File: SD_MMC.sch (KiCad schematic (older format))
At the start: 14 parts, among them J3 Micro_SD_Card, U1 MIMX8MM6DVTLZAA, U5 SDINBDG4-8G

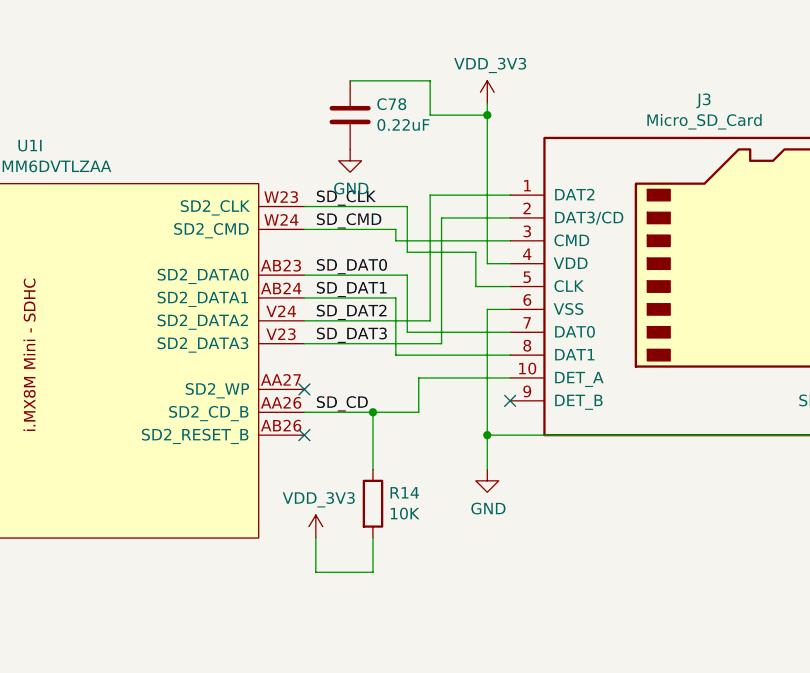
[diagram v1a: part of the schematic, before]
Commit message: Add esd protection for usb
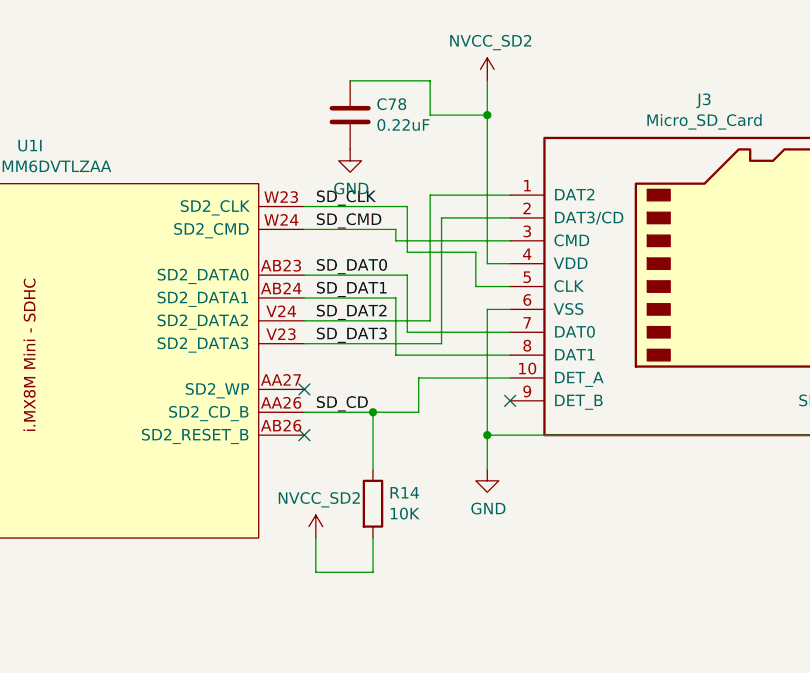
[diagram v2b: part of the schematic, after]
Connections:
- net VDD_3V3: no longer C78.1, J3.4 (VDD), R14.2
- new net NVCC_SD2: C78.1, J3.4 (VDD), R14.2
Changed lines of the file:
@@
 	1    0    0    -1
 $EndComp
-$Comp
-L mxenc:VDD_3V3 #PWR0142
-U 1 1 5D204D73
-P 10200 4150
-F 0 "#PWR0142" H 10200 4000 50  0001 C CNN
-F 1 "VDD_3V3" H 10215 4323 50  0000 C CNN
-F 2 "" H 10200 4150 50  0001 C CNN
-F 3 "" H 10200 4150 50  0001 C CNN
-	1    10200 4150
-	1    0    0    -1
-$EndComp
-Wire Wire Line
-	10200 4150 10200 4200
 Wire Wire Line
 	10200 4850 10300 4850
@@
 Wire Wire Line
 	9700 5750 9700 5500
-$Comp
-L mxenc:VDD_3V3 #PWR0144
-U 1 1 5D211DBD
-P 9450 6050
-F 0 "#PWR0144" H 9450 5900 50  0001 C CNN
-F 1 "VDD_3V3" H 9465 6223 50  0000 C CNN
-F 2 "" H 9450 6050 50  0001 C CNN
-F 3 "" H 9450 6050 50  0001 C CNN
-	1    9450 6050
-	1    0    0    -1
-$EndComp
 Wire Wire Line
 	9450 6050 9450 6200
@@
 NoConn ~ 9400 5400
 NoConn ~ 10300 5450
+$Comp
+L mxenc:NVCC_SD2 #PWR0144
+U 1 1 5DC50CF4
+P 10200 4050
+F 0 "#PWR0144" H 10200 3900 50  0001 C CNN
+F 1 "NVCC_SD2" H 10215 4223 50  0000 C CNN
+F 2 "" H 10200 4050 50  0001 C CNN
+F 3 "" H 10200 4050 50  0001 C CNN
+	1    10200 4050
+	1    0    0    -1
+$EndComp
+Wire Wire Line
+	10200 4050 10200 4200
+$Comp
+L mxenc:NVCC_SD2 #PWR0243
+U 1 1 5DC5A2D8
+P 9450 6050
+F 0 "#PWR0243" H 9450 5900 50  0001 C CNN
+F 1 "NVCC_SD2" H 9465 6223 50  0000 C CNN
+F 2 "" H 9450 6050 50  0001 C CNN
+F 3 "" H 9450 6050 50  0001 C CNN
+	1    9450 6050
+	1    0    0    -1
+$EndComp
 $EndSCHEMATC

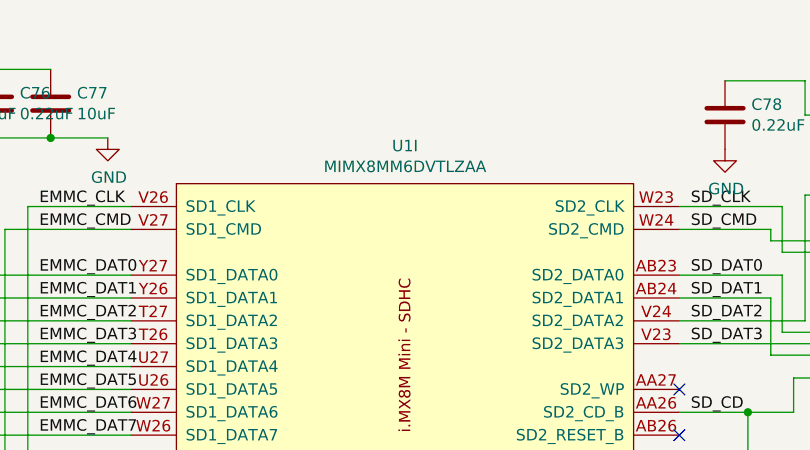
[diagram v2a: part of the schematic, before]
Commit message: Complete entry of bom
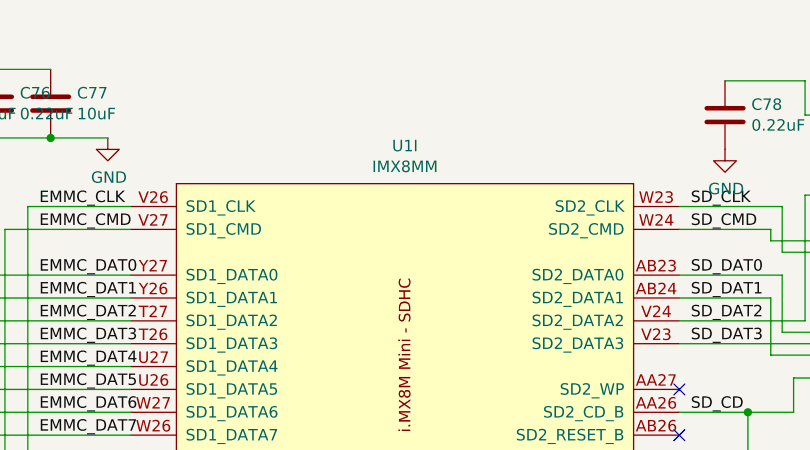
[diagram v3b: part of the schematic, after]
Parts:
- C71: Mfgr (none) -> Murata; Part (none) -> GRM155C80J475MEAAD; Vendorpart (none) -> 490-14458-1-ND
- C72, C73, C74, C75, C76, C80: Mfgr (none) -> Murata; Part (none) -> GRM033C80J224KE90D; Vendorpart (none) -> 490-10392-1-ND
- C77: Mfgr (none) -> Murata; Part (none) -> GRM155C80J106ME11D; Vendorpart (none) -> 490-13233-1-ND
- C78: Mfgr (none) -> Murata; Part (none) -> GRM155C8YA224ME01D; Vendorpart (none) -> 490-10446-1-ND
- C79: Mfgr (none) -> Murata; Part (none) -> GRM155C81A105KA12D; Vendorpart (none) -> 490-12699-1-ND
- J3: Mfgr (none) -> Amphenol; Part (none) -> 114-00841-68; Vendorpart (none) -> 114-00841-68-1-ND
- R14: Mfgr (none) -> Panasonic; Part (none) -> ERJ-2GEJ103X; Vendorpart (none) -> P10KJCT-ND
- U1: value MIMX8MM6DVTLZAA -> IMX8MM; Mfgr (none) -> NXP; Part (none) -> MIMX8MM6CVTKZAA; Vendorpart (none) -> 568-15276-ND
- U5: Field4 SDINBDG4-8G -> (none); Field5 SanDisk -> (none); Field6 Unavailable -> (none); Field7 USB Flash Drives 8GB 3.3V -> (none); Field8 None -> (none); Mfgr (none) -> SanDisk; Part (none) -> SDINBDG4-8G-I1; Vendor (none) -> Mouser; Vendorpart (none) -> 467-SDINBDG4-8G-I1
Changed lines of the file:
@@
 P 8200 7200
 F 0 "U1" H 8200 10065 50  0000 C CNN
-F 1 "MIMX8MM6DVTLZAA" H 8200 9974 50  0000 C CNN
+F 1 "IMX8MM" H 8200 9974 50  0000 C CNN
 F 2 "mxenc:BGA-729_27x27_14.0x14.0mm" H 8450 9950 50  0001 C CNN
 F 3 "" H 7450 9950 50  0001 C CNN
+F 4 "NXP" H 8200 7200 50  0001 C CNN "Mfgr"
+F 5 "MIMX8MM6CVTKZAA" H 8200 7200 50  0001 C CNN "Part"
+F 6 "568-15276-ND" H 8200 7200 50  0001 C CNN "Vendorpart"
 	9    8200 7200
 	1    0    0    -1
@@
 F 2 "mxenc:BGA153C50P14X14_1300X1150X80N" H 4950 5500 50  0001 L BNN
 F 3 "" H 4950 5500 50  0001 L BNN
-F 4 "SDINBDG4-8G" H 4950 5500 50  0001 L BNN "Field4"
-F 5 "SanDisk" H 4950 5500 50  0001 L BNN "Field5"
-F 6 "Unavailable" H 4950 5500 50  0001 L BNN "Field6"
-F 7 "USB Flash Drives 8GB 3.3V" H 4950 5500 50  0001 L BNN "Field7"
-F 8 "None" H 4950 5500 50  0001 L BNN "Field8"
+F 4 "SanDisk" H 4950 5500 50  0001 C CNN "Mfgr"
+F 5 "SDINBDG4-8G-I1" H 4950 5500 50  0001 C CNN "Part"
+F 6 "Mouser" H 4950 5500 50  0001 C CNN "Vendor"
+F 7 "467-SDINBDG4-8G-I1" H 4950 5500 50  0001 C CNN "Vendorpart"
 	1    4950 5500
 	1    0    0    -1
@@
 F 2 "Resistor_SMD:R_0402_1005Metric" V 9630 5900 50  0001 C CNN
 F 3 "~" H 9700 5900 50  0001 C CNN
+F 4 "Panasonic" H 9700 5900 50  0001 C CNN "Mfgr"
+F 5 "ERJ-2GEJ103X" H 9700 5900 50  0001 C CNN "Part"
+F 6 "P10KJCT-ND" H 9700 5900 50  0001 C CNN "Vendorpart"
 	1    9700 5900
 	1    0    0    -1
@@
 F 2 "Capacitor_SMD:C_0402_1005Metric" H 9638 4050 50  0001 C CNN
 F 3 "~" H 9600 4200 50  0001 C CNN
+F 4 "Murata" H 9600 4200 50  0001 C CNN "Mfgr"
+F 5 "GRM155C8YA224ME01D" H 9600 4200 50  0001 C CNN "Part"
+F 6 "490-10446-1-ND" H 9600 4200 50  0001 C CNN "Vendorpart"
 	1    9600 4200
 	1    0    0    -1
@@
 F 2 "Capacitor_SMD:C_0201_0603Metric" H 5888 4000 50  0001 C CNN
 F 3 "~" H 5850 4150 50  0001 C CNN
+F 4 "Murata" H 5850 4150 50  0001 C CNN "Mfgr"
+F 5 "GRM033C80J224KE90D" H 5850 4150 50  0001 C CNN "Part"
+F 6 "490-10392-1-ND" H 5850 4150 50  0001 C CNN "Vendorpart"
 	1    5850 4150
 	1    0    0    -1
@@
 F 2 "Capacitor_SMD:C_0201_0603Metric" H 6188 4000 50  0001 C CNN
 F 3 "~" H 6150 4150 50  0001 C CNN
+F 4 "Murata" H 6150 4150 50  0001 C CNN "Mfgr"
+F 5 "GRM033C80J224KE90D" H 6150 4150 50  0001 C CNN "Part"
+F 6 "490-10392-1-ND" H 6150 4150 50  0001 C CNN "Vendorpart"
 	1    6150 4150
 	1    0    0    -1
@@
 F 2 "Capacitor_SMD:C_0201_0603Metric" H 6438 4000 50  0001 C CNN
 F 3 "~" H 6400 4150 50  0001 C CNN
+F 4 "Murata" H 6400 4150 50  0001 C CNN "Mfgr"
+F 5 "GRM033C80J224KE90D" H 6400 4150 50  0001 C CNN "Part"
+F 6 "490-10392-1-ND" H 6400 4150 50  0001 C CNN "Vendorpart"
 	1    6400 4150
 	1    0    0    -1
@@
 F 2 "Capacitor_SMD:C_0402_1005Metric" H 6688 4000 50  0001 C CNN
 F 3 "~" H 6650 4150 50  0001 C CNN
+F 4 "Murata" H 6650 4150 50  0001 C CNN "Mfgr"
+F 5 "GRM155C80J106ME11D" H 6650 4150 50  0001 C CNN "Part"
+F 6 "490-13233-1-ND" H 6650 4150 50  0001 C CNN "Vendorpart"
 	1    6650 4150
 	1    0    0    -1
@@
 F 2 "Capacitor_SMD:C_0201_0603Metric" H 4138 4000 50  0001 C CNN
 F 3 "~" H 4100 4150 50  0001 C CNN
+F 4 "Murata" H 4100 4150 50  0001 C CNN "Mfgr"
+F 5 "GRM033C80J224KE90D" H 4100 4150 50  0001 C CNN "Part"
+F 6 "490-10392-1-ND" H 4100 4150 50  0001 C CNN "Vendorpart"
 	1    4100 4150
 	1    0    0    -1
@@
 F 2 "Capacitor_SMD:C_0201_0603Metric" H 3888 4000 50  0001 C CNN
 F 3 "~" H 3850 4150 50  0001 C CNN
+F 4 "Murata" H 3850 4150 50  0001 C CNN "Mfgr"
+F 5 "GRM033C80J224KE90D" H 3850 4150 50  0001 C CNN "Part"
+F 6 "490-10392-1-ND" H 3850 4150 50  0001 C CNN "Vendorpart"
 	1    3850 4150
 	1    0    0    -1
@@
 F 2 "Capacitor_SMD:C_0402_1005Metric" H 3638 4000 50  0001 C CNN
 F 3 "~" H 3600 4150 50  0001 C CNN
+F 4 "Murata" H 3600 4150 50  0001 C CNN "Mfgr"
+F 5 "GRM155C80J475MEAAD" H 3600 4150 50  0001 C CNN "Part"
+F 6 "490-14458-1-ND" H 3600 4150 50  0001 C CNN "Vendorpart"
 	1    3600 4150
 	1    0    0    -1
@@
 F 2 "Capacitor_SMD:C_0201_0603Metric" H 3688 5000 50  0001 C CNN
 F 3 "~" H 3650 5150 50  0001 C CNN
+F 4 "Murata" H 3650 5150 50  0001 C CNN "Mfgr"
+F 5 "GRM033C80J224KE90D" H 3650 5150 50  0001 C CNN "Part"
+F 6 "490-10392-1-ND" H 3650 5150 50  0001 C CNN "Vendorpart"
 	1    3650 5150
 	1    0    0    -1
@@
 F 2 "Capacitor_SMD:C_0402_1005Metric" H 3438 5000 50  0001 C CNN
 F 3 "~" H 3400 5150 50  0001 C CNN
+F 4 "Murata" H 3400 5150 50  0001 C CNN "Mfgr"
+F 5 "GRM155C81A105KA12D" H 3400 5150 50  0001 C CNN "Part"
+F 6 "490-12699-1-ND" H 3400 5150 50  0001 C CNN "Vendorpart"
 	1    3400 5150
 	1    0    0    -1
@@
 F 2 "mxenc:114-00841-68" H 12350 5250 50  0001 C CNN
 F 3 "http://katalog.we-online.de/em/datasheet/693072010801.pdf" H 11200 4950 50  0001 C CNN
+F 4 "Amphenol" H 11200 4950 50  0001 C CNN "Mfgr"
+F 5 "114-00841-68" H 11200 4950 50  0001 C CNN "Part"
+F 6 "114-00841-68-1-ND" H 11200 4950 50  0001 C CNN "Vendorpart"
 	1    11200 4950
 	1    0    0    -1

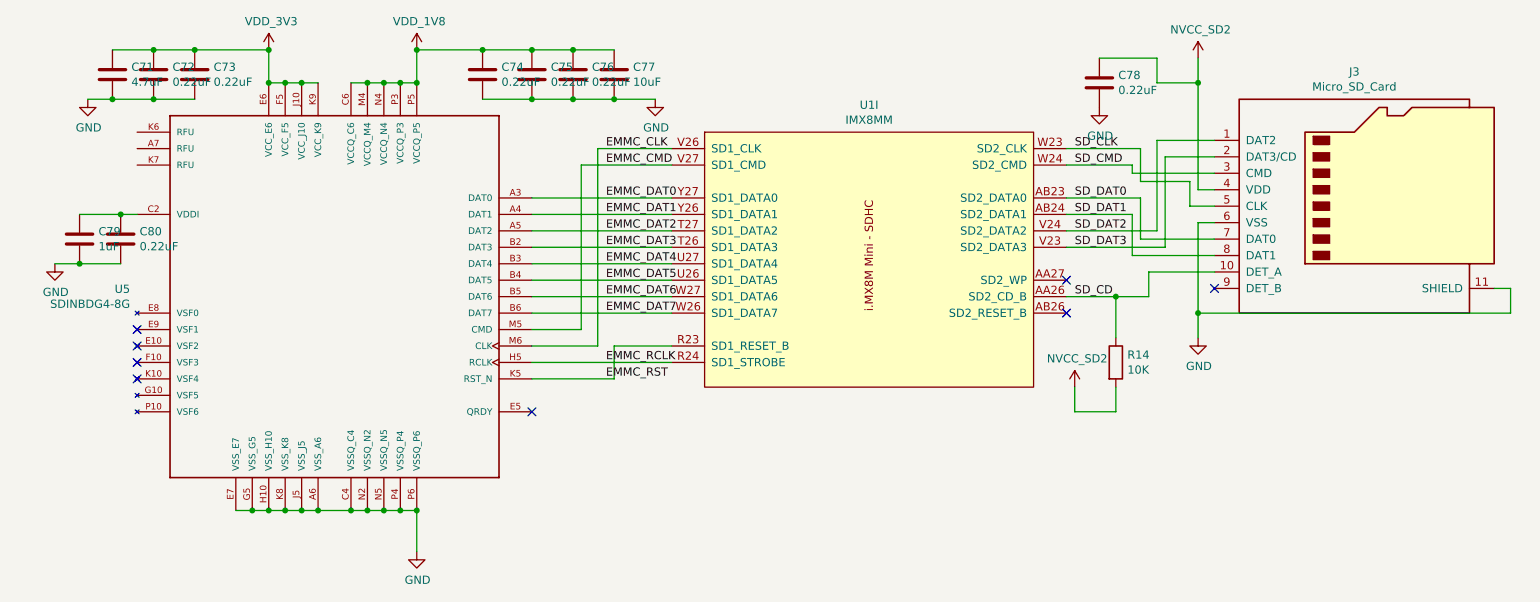
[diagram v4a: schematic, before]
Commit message: rough layout, routing for emmc and csi, dsi, pcie
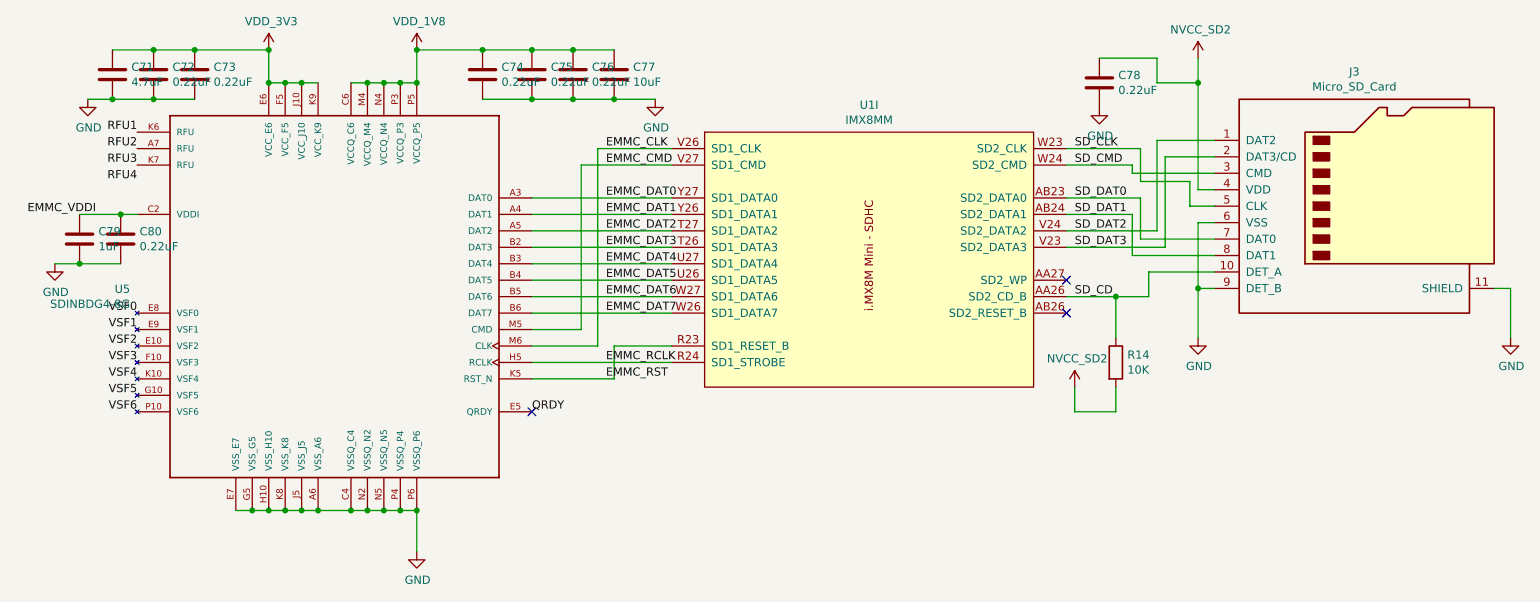
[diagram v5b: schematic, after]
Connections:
- net GND: now also J3.9 (DET_B)
- net RFU2: now reaches U5.A7 (RFU)
- net EMMC_VDDI: now reaches C79.1, C80.1, U5.C2 (VDDI)
- net VSF2: now reaches U5.E10 (VSF2)
- net QRDY: now reaches U5.E5 (QRDY)
- net VSF0: now reaches U5.E8 (VSF0)
- net VSF1: now reaches U5.E9 (VSF1)
- net VSF3: now reaches U5.F10 (VSF3)
- net VSF5: now reaches U5.G10 (VSF5)
- net VSF4: now reaches U5.K10 (VSF4)
- net RFU1: now reaches U5.K6 (RFU)
- net RFU3: now reaches U5.K7 (RFU)
- net VSF6: now reaches U5.P10 (VSF6)
- no-connect marks 8 -> 3
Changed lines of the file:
@@
-	1    0    0    -1
-$EndComp
-$Comp
-L mxenc:SDINBDG4-8G U5
-U 1 1 5D196F4B
-P 4950 5500
-F 0 "U5" H 3707 5546 50  0000 R CNN
-F 1 "SDINBDG4-8G" H 3707 5455 50  0000 R CNN
-F 2 "mxenc:BGA153C50P14X14_1300X1150X80N" H 4950 5500 50  0001 L BNN
-F 3 "" H 4950 5500 50  0001 L BNN
-F 4 "SanDisk" H 4950 5500 50  0001 C CNN "Mfgr"
-F 5 "SDINBDG4-8G-I1" H 4950 5500 50  0001 C CNN "Part"
-F 6 "Mouser" H 4950 5500 50  0001 C CNN "Vendor"
-F 7 "467-SDINBDG4-8G-I1" H 4950 5500 50  0001 C CNN "Vendorpart"
-	1    4950 5500
 	1    0    0    -1
 $EndComp
@@
 Wire Wire Line
 	5450 4200 5350 4200
-Connection ~ 4450 6800
-Wire Wire Line
-	4450 6800 4350 6800
-Wire Wire Line
-	4550 6800 4450 6800
 Connection ~ 4550 6800
 Wire Wire Line
@@
 Wire Wire Line
 	3400 5300 3250 5300
-NoConn ~ 3750 5700
-NoConn ~ 3750 5800
-NoConn ~ 3750 5900
-NoConn ~ 3750 6000
-Wire Wire Line
-	10200 5050 10200 5600
+Wire Wire Line
+	10200 5050 10200 5450
 $Comp
 L Connector:Micro_SD_Card_Det J3
@@
 Wire Wire Line
 	12000 5450 12100 5450
-Wire Wire Line
-	12100 5450 12100 5600
-Wire Wire Line
-	12100 5600 10200 5600
-Connection ~ 10200 5600
-Wire Wire Line
-	10200 5600 10200 5750
 Connection ~ 9700 5500
 Wire Wire Line
@@
 NoConn ~ 9400 5600
 NoConn ~ 9400 5400
-NoConn ~ 10300 5450
 $Comp
 L mxenc:NVCC_SD2 #PWR0144
@@
 	1    0    0    -1
 $EndComp
+Wire Wire Line
+	4550 6800 4450 6800
+Wire Wire Line
+	4450 6800 4350 6800
+Connection ~ 4450 6800
+$Comp
+L mxenc:SDINBDG4-8G U5
+U 1 1 5D196F4B
+P 4950 5500
+F 0 "U5" H 3707 5546 50  0000 R CNN
+F 1 "SDINBDG4-8G" H 3707 5455 50  0000 R CNN
+F 2 "mxenc:BGA153C50P14X14_1300X1150X80N" H 4950 5500 50  0001 L BNN
+F 3 "" H 4950 5500 50  0001 L BNN
+F 4 "SanDisk" H 4950 5500 50  0001 C CNN "Mfgr"
+F 5 "SDINBDG4-8G-I1" H 4950 5500 50  0001 C CNN "Part"
+F 6 "Mouser" H 4950 5500 50  0001 C CNN "Vendor"
+F 7 "467-SDINBDG4-8G-I1" H 4950 5500 50  0001 C CNN "Vendorpart"
+	1    4950 5500
+	1    0    0    -1
+$EndComp
+Text Label 3750 4500 2    50   ~ 0
+RFU1
+Text Label 3750 4600 2    50   ~ 0
+RFU2
+Text Label 3750 4800 2    50   ~ 0
+RFU4
+Text Label 3750 5600 2    50   ~ 0
+VSF0
+Text Label 3750 5700 2    50   ~ 0
+VSF1
+Text Label 3750 5800 2    50   ~ 0
+VSF2
+Text Label 3750 5900 2    50   ~ 0
+VSF3
+Text Label 3750 6000 2    50   ~ 0
+VSF4
+Text Label 3750 6100 2    50   ~ 0
+VSF5
+Text Label 3750 6200 2    50   ~ 0
+VSF6
+Text Label 6150 6200 0    50   ~ 0
+QRDY
+Text Label 3750 4700 2    50   ~ 0
+RFU3
+Text Label 3500 5000 2    50   ~ 0
+EMMC_VDDI
+Wire Wire Line
+	10300 5450 10200 5450
+Connection ~ 10200 5450
+Wire Wire Line
+	10200 5450 10200 5750
+$Comp
+L power:GND #PWR0150
+U 1 1 5E2D7AF8
+P 12100 5750
+F 0 "#PWR0150" H 12100 5500 50  0001 C CNN
+F 1 "GND" H 12105 5577 50  0000 C CNN
+F 2 "" H 12100 5750 50  0001 C CNN
+F 3 "" H 12100 5750 50  0001 C CNN
+	1    12100 5750
+	1    0    0    -1
+$EndComp
+Wire Wire Line
+	12100 5450 12100 5750
 $EndSCHEMATC

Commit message: Cleanup remaining DRC problems from schematic
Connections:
- no-connect marks 3 -> 6
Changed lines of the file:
@@
 Text Label 3750 4600 2    50   ~ 0
 RFU2
-Text Label 3750 4800 2    50   ~ 0
-RFU4
 Text Label 3750 5600 2    50   ~ 0
 VSF0
@@
 Wire Wire Line
 	12100 5450 12100 5750
+NoConn ~ 3750 4500
+NoConn ~ 3750 4700
+NoConn ~ 3750 4600
 $EndSCHEMATC
